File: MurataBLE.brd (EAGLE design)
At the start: 70 x 92 mm, 43 parts, among them CON1 C-2235, IC1 I-5448, IC3 74LVC1G00DBV, Q1 FC-135 32.7680KA-AG3, Q2 12MHz, SW1 P8073, SW2 P8073, SW3 P8073, U1 IC_BLE_LBCA2HNZYZ-711, X1 TSW-114-02-S-S

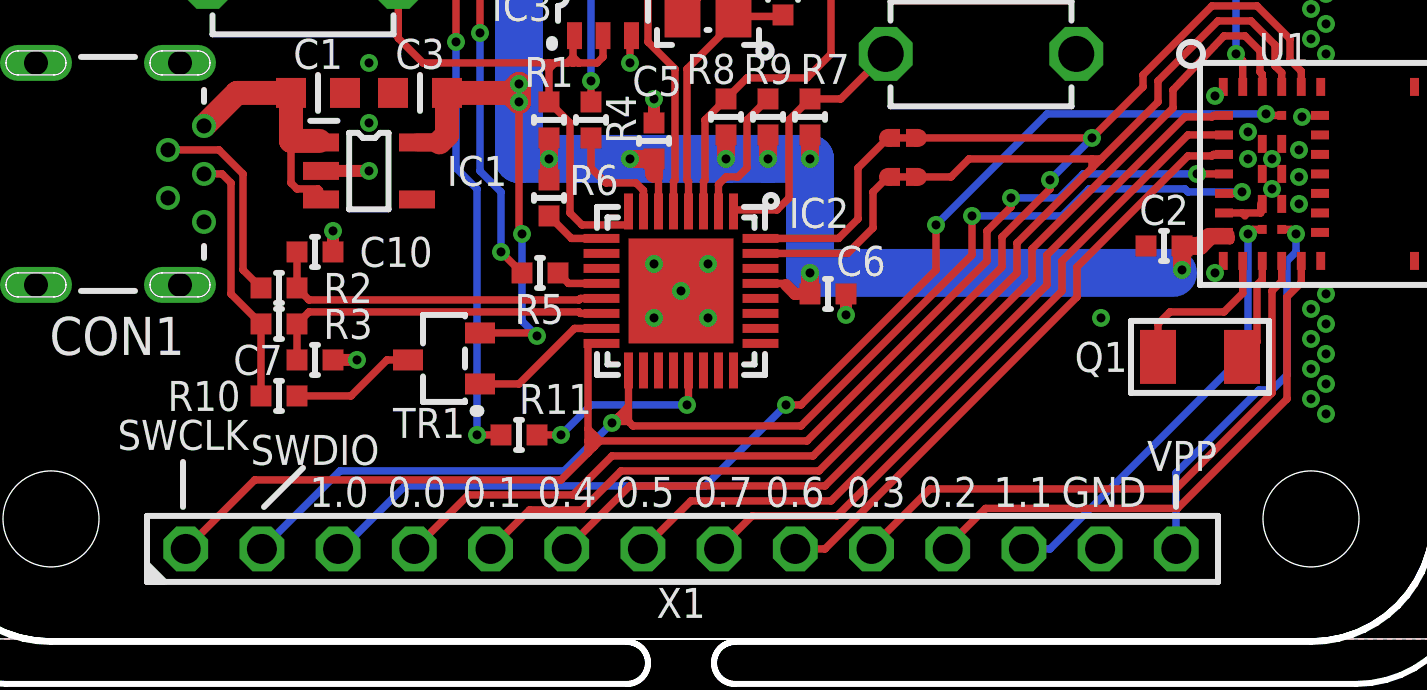
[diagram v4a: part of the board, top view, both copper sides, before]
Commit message: [ USB ] R11 moved
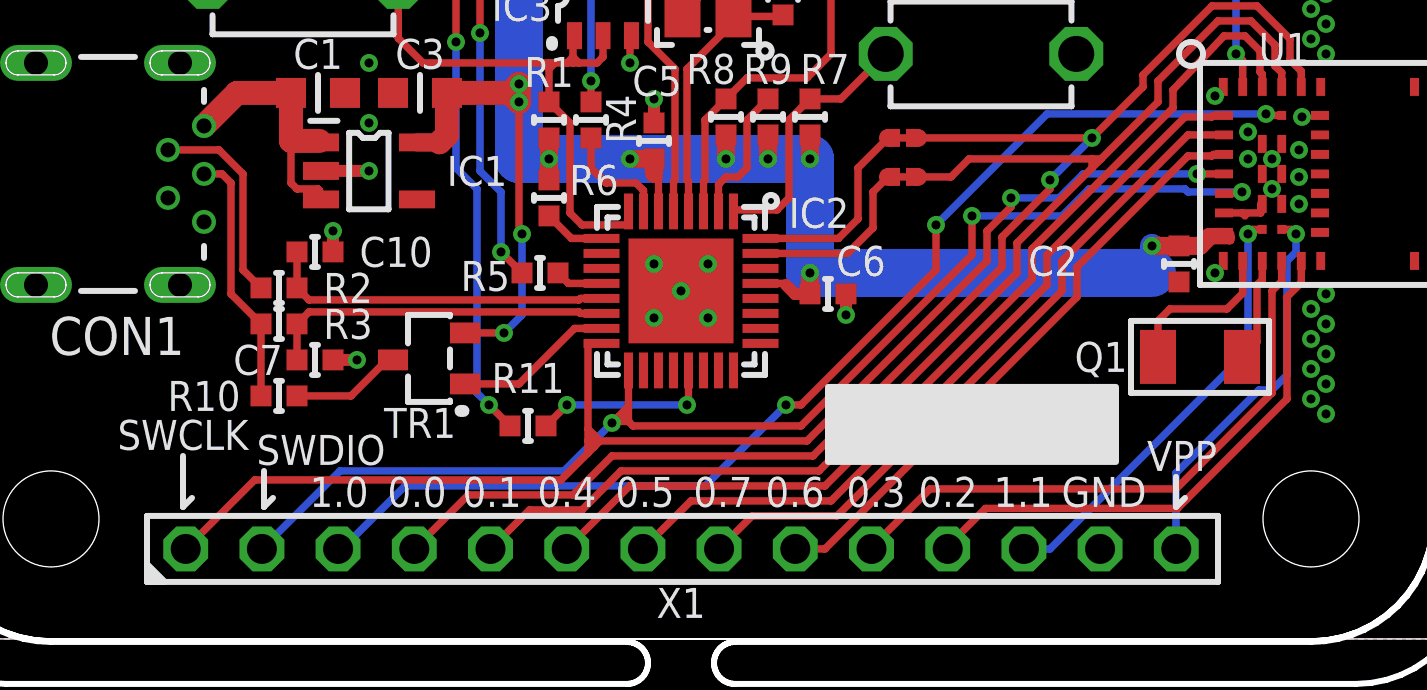
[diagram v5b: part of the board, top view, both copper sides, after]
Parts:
- moved C2 0.78 mm to (51.6, 22.5), turned to 270 degrees
- moved TR1 0.50 mm to (26.6, 19.3)
- moved R11 0.42 mm to (29.9, 17.1)
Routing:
- net 3.3V: track 65.9 -> 64.9 mm
- net N$13: track 21.4 -> 20.7 mm
- net N$7: track 4.82 -> 5.32 mm
- net N$6: track 4.20 -> 3.70 mm
- net GND: vias 46 -> 45

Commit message: [ USB ] UART connection
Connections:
- net P0_0: no longer TP3.TP, TP8.TP
- net P0_1: no longer TP4.TP, TP7.TP
- net TGT_RX: now also TP4.TP, TP7.TP
- net TGT_TX: now also TP3.TP, TP8.TP
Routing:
- net P0_1: track 45.9 -> 39.9 mm
- net P0_0: track 43.1 -> 41.8 mm
- net TGT_TX: track 6.21 -> 7.01 mm
- net TGT_RX: track 6.83 -> 7.63 mm
- net N$15: track 0.60 -> 0.00 mm
- net N$14: track 0.60 -> 0.00 mm
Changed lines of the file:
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@@
 <wire x1="29.95" y1="14.3" x2="31.7" y2="14.3" width="0.25" layer="1"/>
 <wire x1="31.7" y1="14.3" x2="33" y2="15.6" width="0.25" layer="1"/>
-<contactref element="TP8" pad="TP"/>
-<wire x1="42.7" y1="25.4" x2="42.9" y2="25.4" width="0.25" layer="1"/>
-<wire x1="44" y1="25.4" x2="42.9" y2="25.4" width="0.25" layer="1"/>
 <wire x1="39.6" y1="15.6" x2="46.2" y2="22.2" width="0.25" layer="1"/>
 <wire x1="46.2" y1="22.2" x2="46.2" y2="23.2" width="0.25" layer="1"/>
 <contactref element="X1" pad="5"/>
-<contactref element="TP3" pad="TP"/>
 </signal>
 <signal name="P0_1">
@@
 <wire x1="27.91" y1="14.8" x2="31.4" y2="14.8" width="0.25" layer="1"/>
 <wire x1="31.4" y1="14.8" x2="32.7" y2="16.1" width="0.25" layer="1"/>
-<wire x1="48.7" y1="26.7" x2="42.9" y2="26.7" width="0.25" layer="1"/>
-<contactref element="TP7" pad="TP"/>
-<wire x1="42.9" y1="26.7" x2="42.7" y2="26.7" width="0.25" layer="1"/>
 <wire x1="39.4" y1="16.1" x2="45.7" y2="22.4" width="0.25" layer="1"/>
 <contactref element="X1" pad="4"/>
-<contactref element="TP4" pad="TP"/>
 </signal>
 <signal name="P0_2">
@@
 <wire x1="41.4" y1="24.9" x2="41.9" y2="25.4" width="0.25" layer="1"/>
 <contactref element="TP1" pad="TP"/>
-</signal>
-<signal name="TGT_RX">
-<contactref element="IC2" pad="32"/>
-<wire x1="40.9" y1="25.7" x2="40.9" y2="24" width="0.25" layer="1"/>
-<wire x1="37.65" y1="23.35" x2="40.25" y2="23.35" width="0.25" layer="1"/>
-<wire x1="40.25" y1="23.35" x2="40.9" y2="24" width="0.25" layer="1"/>
-<contactref element="TP6" pad="TP"/>
-<wire x1="42.1" y1="26.7" x2="41.9" y2="26.7" width="0.25" layer="1"/>
-<wire x1="40.9" y1="25.7" x2="41.9" y2="26.7" width="0.25" layer="1"/>
-<contactref element="TP2" pad="TP"/>
+<contactref element="TP8" pad="TP"/>
+<contactref element="TP3" pad="TP"/>
+<wire x1="42.7" y1="25.4" x2="42.9" y2="25.4" width="0.25" layer="1"/>
+<wire x1="42.7" y1="25.4" x2="42.1" y2="25.4" width="0.25" layer="1"/>
 </signal>
 <signal name="N$4">
@@
 <wire x1="28.2" y1="18.2" x2="28.2" y2="25" width="0.25" layer="16"/>
 </signal>
-<signal name="N$14">
+<signal name="TGT_RX">
+<contactref element="TP7" pad="TP"/>
+<contactref element="TP4" pad="TP"/>
+<contactref element="IC2" pad="32"/>
+<contactref element="TP6" pad="TP"/>
+<contactref element="TP2" pad="TP"/>
+<wire x1="42.9" y1="26.7" x2="42.7" y2="26.7" width="0.25" layer="1"/>
+<wire x1="40.9" y1="25.7" x2="40.9" y2="24" width="0.25" layer="1"/>
+<wire x1="37.65" y1="23.35" x2="40.25" y2="23.35" width="0.25" layer="1"/>
+<wire x1="40.25" y1="23.35" x2="40.9" y2="24" width="0.25" layer="1"/>
+<wire x1="42.1" y1="26.7" x2="41.9" y2="26.7" width="0.25" layer="1"/>
+<wire x1="40.9" y1="25.7" x2="41.9" y2="26.7" width="0.25" layer="1"/>
 <wire x1="42.1" y1="26.7" x2="42.7" y2="26.7" width="0.25" layer="1"/>
 </signal>
-<signal name="N$15">
-<wire x1="42.1" y1="25.4" x2="42.7" y2="25.4" width="0.25" layer="1"/>
-</signal>
 </signals>

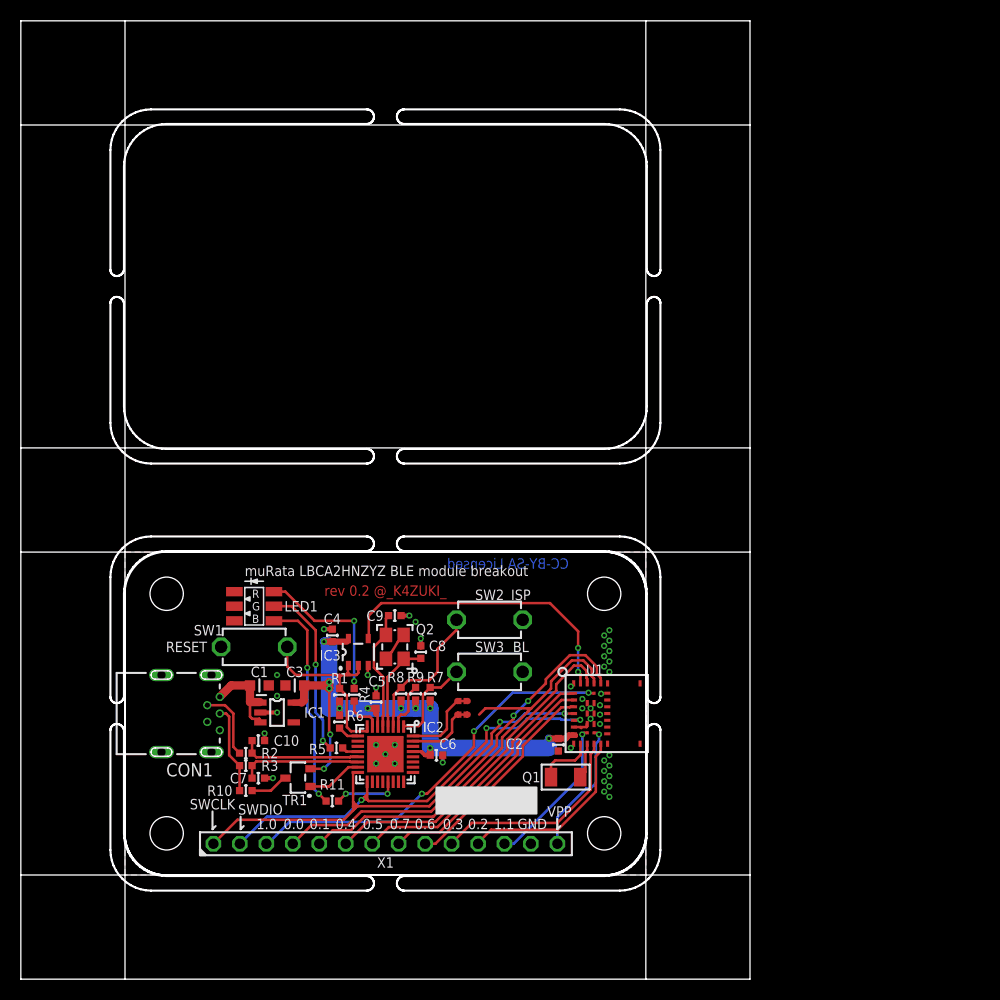
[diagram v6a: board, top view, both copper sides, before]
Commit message: [ USB ] Fiducials; panel direction
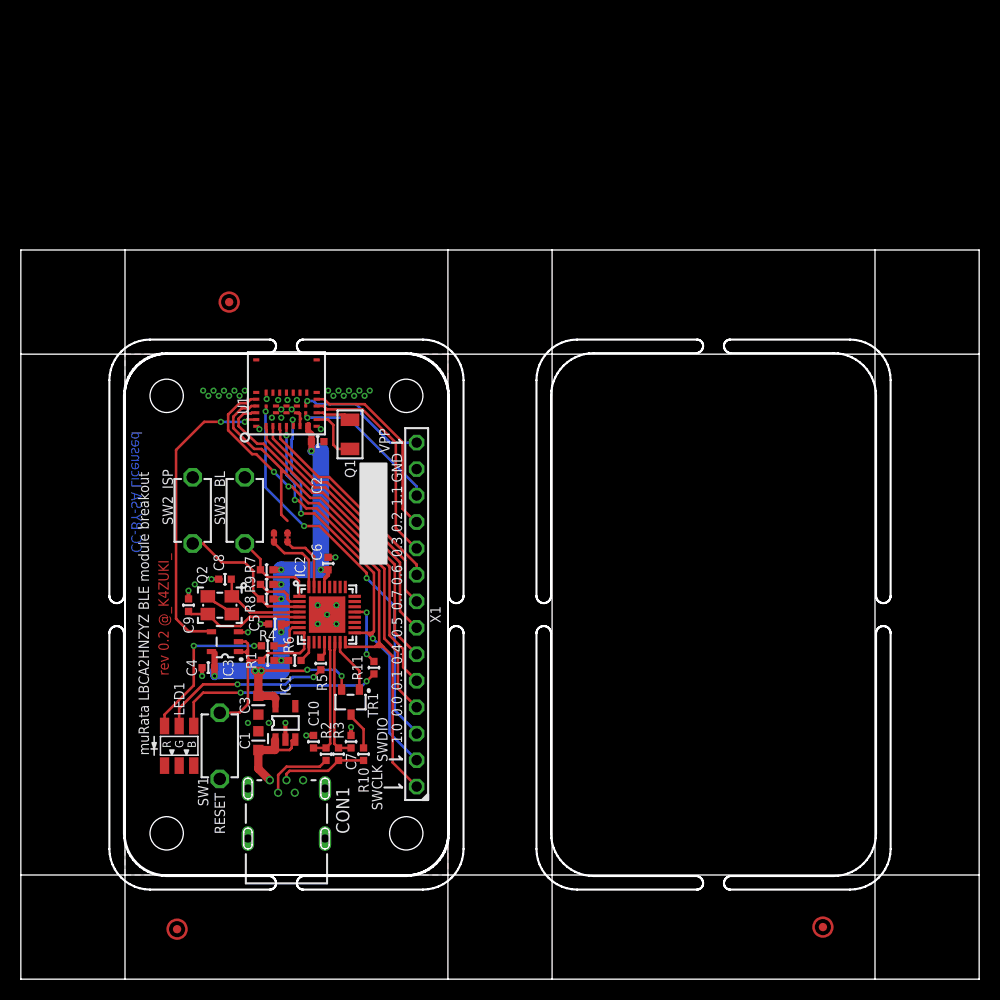
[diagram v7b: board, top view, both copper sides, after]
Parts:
- added TP10, TP11, TP9: TPTP08R, testpad_local:TP08R
- moved Q1 38.9 mm to (31.6, 52.3), turned to 90 degrees
- moved U1 38.5 mm to (22.0, 52.5), turned to 0 degrees
- moved C2 37.2 mm to (28.5, 51.6), turned to 0 degrees
- moved SW2 30.4 mm to (16.5, 45.0), turned to 270 degrees
- moved SW3 28.2 mm to (21.5, 45.0), turned to 270 degrees
- moved TP7 24.7 mm to (24.3, 42.9), turned to 90 degrees
- moved TP8 24.6 mm to (25.6, 42.9), turned to 90 degrees
- moved TP4 24.4 mm to (24.3, 42.7), turned to 90 degrees
- moved TP3 24.3 mm to (25.6, 42.7), turned to 90 degrees
- moved TP2 23.5 mm to (24.3, 42.1), turned to 90 degrees
- moved TP1 23.5 mm to (25.6, 42.1), turned to 90 degrees
- moved TP6 23.3 mm to (24.3, 41.9), turned to 90 degrees
- moved TP5 23.2 mm to (25.6, 41.9), turned to 90 degrees
- moved X1 22.2 mm to (38.0, 35.0), turned to 270 degrees
- moved C6 21.1 mm to (29.5, 39.9), turned to 90 degrees
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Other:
- board size 70 x 92 mm -> 92 x 70 mm
